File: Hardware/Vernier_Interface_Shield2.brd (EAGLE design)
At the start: 76.2 x 71.1 mm, 45 parts, among them U1 74HC4052SO, U2 LMV358SOICT

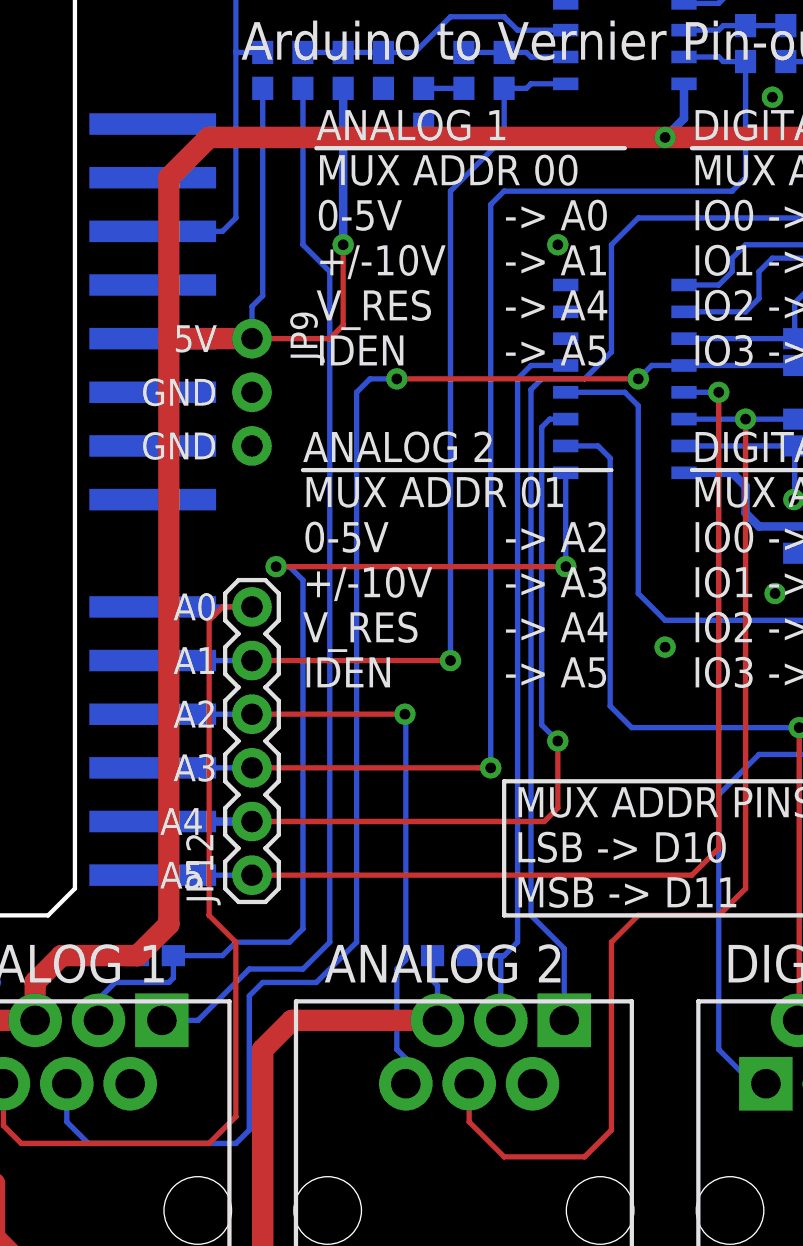
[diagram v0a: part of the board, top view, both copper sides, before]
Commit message: Updated the Top layer Silk
Updated top layer silk to have A0-A5 next to the exposed vias. Moved the
exposed vias for 5V and GND to line up with A0-A5.
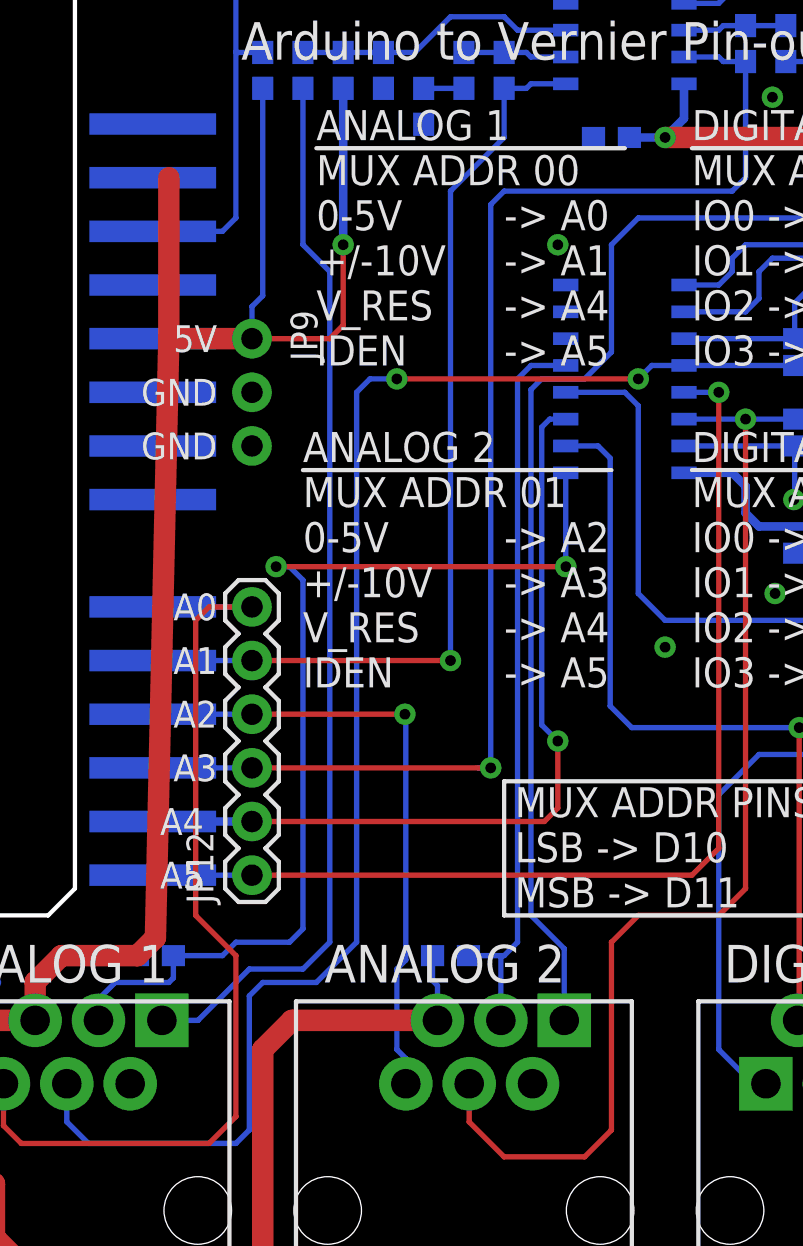
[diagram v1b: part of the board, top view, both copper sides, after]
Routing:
- net 5V: track 293.6 -> 269.1 mm
- net AS1_AN2: track 44.9 -> 45.8 mm
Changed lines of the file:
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@@
 <grid distance="0.025" unitdist="inch" unit="inch" style="lines" multiple="1" display="yes" altdistance="0.005" altunitdist="inch" altunit="inch"/>
 <layers>
-<layer number="1" name="Top" color="4" fill="1" visible="yes" active="yes"/>
+<layer number="1" name="Top" color="4" fill="1" visible="no" active="yes"/>
 <layer number="16" name="Bottom" color="1" fill="1" visible="yes" active="yes"/>
 <layer number="17" name="Pads" color="2" fill="1" visible="yes" active="yes"/>
@@
 <contactref element="S3" pad="1"/>
 <contactref element="S4" pad="3"/>
+<wire x1="12.775" y1="9.81" x2="31.825" y2="9.81" width="0" layer="19" extent="1-1"/>
 </signal>
 <signal name="5V">
@@
 <wire x1="13.843" y1="45.085" x2="18.542" y2="45.085" width="0.4064" layer="16"/>
 <wire x1="14.605" y1="45.085" x2="18.542" y2="45.085" width="1.016" layer="1"/>
+<wire x1="14.605" y1="45.085" x2="13.97" y2="16.725" width="1.016" layer="1"/>
 <wire x1="13.12" y1="15.875" x2="9.525" y2="15.875" width="0.254" layer="16"/>
 <wire x1="50.8" y1="54.61" x2="38.1" y2="54.61" width="1.016" layer="1"/>
@@
 <wire x1="3.81" y1="11.43" x2="5.19" y2="12.81" width="1.016" layer="1"/>
 <wire x1="8.275" y1="12.81" x2="5.19" y2="12.81" width="1.016" layer="1"/>
+<wire x1="13.97" y1="16.725" x2="13.12" y2="15.875" width="1.016" layer="1"/>
 <wire x1="13.12" y1="15.875" x2="9.525" y2="15.875" width="1.016" layer="1"/>
 <wire x1="9.525" y1="15.875" x2="8.275" y2="14.625" width="1.016" layer="1"/>
@@
 <wire x1="18.542" y1="45.085" x2="18.542" y2="46.609" width="0.254" layer="16"/>
 <wire x1="18.542" y1="46.609" x2="19.05" y2="47.117" width="0.254" layer="16"/>
-<wire x1="38.1" y1="54.61" x2="16.51" y2="54.61" width="1.016" layer="1"/>
-<wire x1="16.51" y1="54.61" x2="14.605" y2="52.705" width="1.016" layer="1"/>
-<wire x1="14.605" y1="45.085" x2="14.605" y2="17.36" width="1.016" layer="1"/>
-<wire x1="14.605" y1="17.36" x2="13.12" y2="15.875" width="1.016" layer="1"/>
+<wire x1="22.86" y1="56.935" x2="36.41" y2="54.61" width="0" layer="19" extent="16-16"/>
 </signal>
 <signal name="3.3V">
@@
 <contactref element="JP5" pad="6"/>
 <contactref element="JP4" pad="6"/>
+<wire x1="15.875" y1="17.78" x2="15.875" y2="31.75" width="0.254" layer="1"/>
+<wire x1="15.875" y1="31.75" x2="16.51" y2="32.385" width="0.254" layer="1"/>
+<wire x1="16.51" y1="32.385" x2="18.542" y2="32.385" width="0.254" layer="1"/>
 <wire x1="18.542" y1="32.385" x2="13.843" y2="32.385" width="0.254" layer="16"/>
-<wire x1="17.78" y1="16.51" x2="17.78" y2="8.255" width="0.254" layer="1"/>
+<wire x1="15.875" y1="17.78" x2="17.78" y2="15.875" width="0.254" layer="1"/>
+<wire x1="17.78" y1="15.875" x2="17.78" y2="8.255" width="0.254" layer="1"/>
 <wire x1="17.78" y1="8.255" x2="16.51" y2="6.985" width="0.254" layer="1"/>
 <wire x1="16.51" y1="6.985" x2="7.62" y2="6.985" width="0.254" layer="1"/>
@@
 <wire x1="6.775" y1="7.83" x2="7.62" y2="6.985" width="0.254" layer="1"/>
 <contactref element="JP12" pad="6"/>
-<wire x1="17.78" y1="16.51" x2="16.51" y2="17.78" width="0.254" layer="1"/>
-<wire x1="16.51" y1="17.78" x2="16.51" y2="31.75" width="0.254" layer="1"/>
-<wire x1="18.542" y1="32.385" x2="17.145" y2="32.385" width="0.254" layer="1"/>
-<wire x1="17.145" y1="32.385" x2="16.51" y2="31.75" width="0.254" layer="1"/>
 </signal>
 <signal name="AS2_AN2">
